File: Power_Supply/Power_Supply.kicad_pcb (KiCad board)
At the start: 2 copper layers, 100 x 100 mm, 61 parts, among them J1 ICSP, J2 Conn_01x01, J3 Conn_01x01, J4 Conn_01x02, SW1 UP, SW2 DW, SW3 V_I_SEL, SW4 O_EN, U1 L78L08_SOT89, U2 ATmega328PB-AU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

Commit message: need to add display
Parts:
- added J5: Conn_01x07, Custom_Vertical_1x_2.54mm_Pin_Header:PinHeader_1x07_P2.54mm_Vertical, F.Cu at (-13.0, 45.0)
- moved C16 145.0 mm to (66.0, 94.0), turned to 180 degrees
- moved R11 139.7 mm to (64.0, 69.0), turned to 90 degrees
- moved C18 137.9 mm to (60.0, 94.0)
- moved C6 137.4 mm to (72.4, 107.8), turned to 90 degrees
- moved R3 134.5 mm to (84.4, 101.0)
- moved C8 134.5 mm to (80.0, 101.0)
- moved R18 134.4 mm to (54.4, 96.0)
- moved C20 133.1 mm to (51.4, 92.0), turned to 90 degrees
- moved R14 130.2 mm to (73.0, 81.0), turned to 180 degrees
- moved R5 127.6 mm to (89.0, 86.9), turned to 90 degrees
- moved R20 121.6 mm to (84.0, 87.0), turned to -90 degrees
- moved R16 120.1 mm to (73.0, 85.0), turned to 180 degrees
- moved R12 119.8 mm to (73.0, 79.0)
- moved R17 119.7 mm to (73.0, 87.0)
- moved C3 117.9 mm to (80.0, 78.0)
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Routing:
- net +VSW: track 0.00 -> 53.4 mm
- net /V_FB: track 0.00 -> 17.9 mm, vias 0 -> 2
- net Net-(C16-Pad2): track 0.00 -> 17.4 mm
- net Net-(C17-Pad2): track 0.00 -> 14.4 mm
- net Net-(C15-Pad2): track 0.00 -> 14.2 mm
- net GND: track 0.00 -> 12.7 mm, vias 0 -> 4
- net Net-(C13-Pad2): track 0.00 -> 11.0 mm
- net +5V: track 0.00 -> 9.13 mm
- net Net-(C6-Pad1): track 0.00 -> 9.03 mm
- net Net-(U4-Pad3): track 0.00 -> 8.44 mm
- net Net-(R9-Pad2): track 0.00 -> 8.44 mm
- net Net-(R8-Pad2): track 0.00 -> 8.44 mm
- net Net-(R6-Pad2): track 0.00 -> 8.44 mm
- net Net-(R10-Pad2): track 0.00 -> 8.44 mm
- net Net-(R16-Pad1): track 0.00 -> 8.02 mm
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- added copper zone on F.Cu, net +VSW
- added copper zone on F.Cu, net Net-(C16-Pad2)
- added copper zone on F.Cu, net Net-(C6-Pad2)
- added copper zone on F.Cu, net Net-(R13-Pad1)
- added copper zone on F.Cu, net VDC

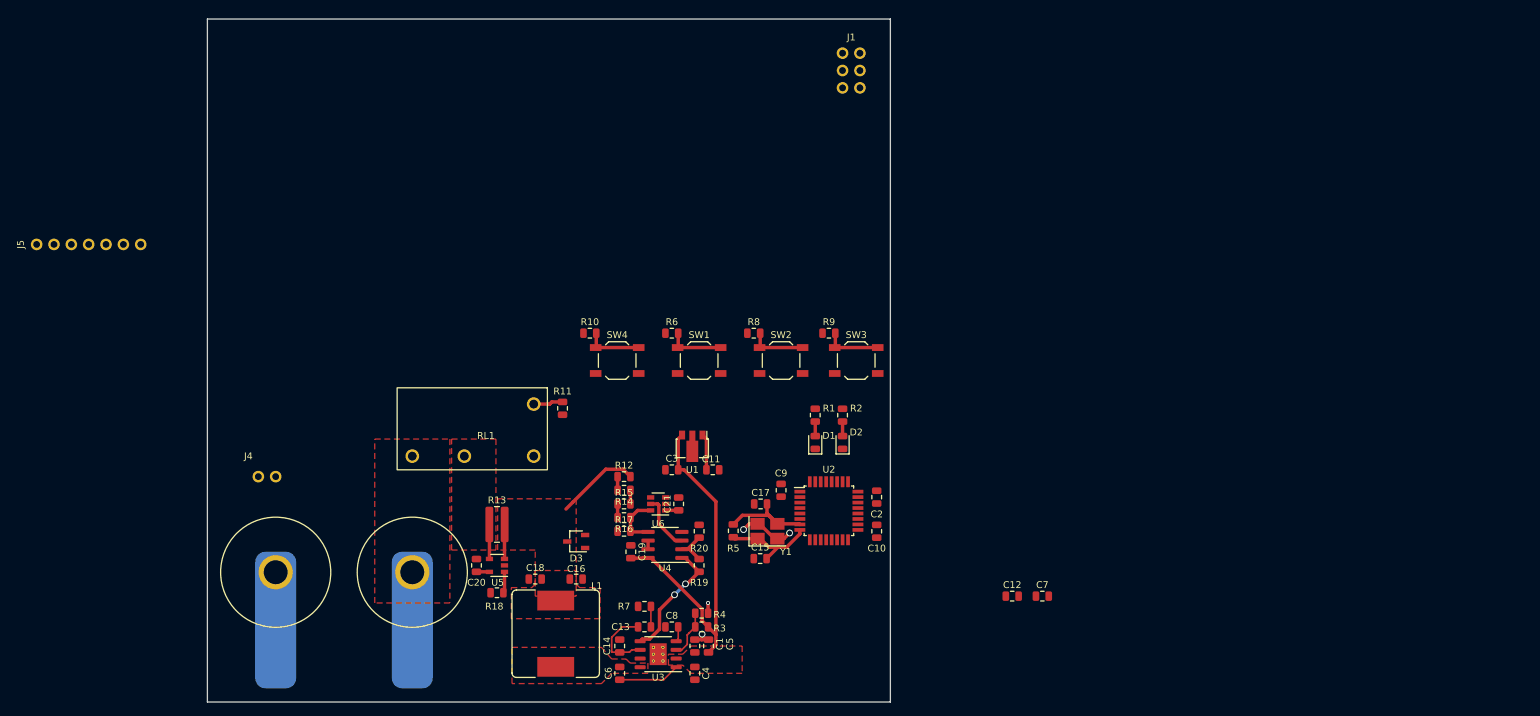
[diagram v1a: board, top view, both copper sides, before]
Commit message: layout complete - OLED missing
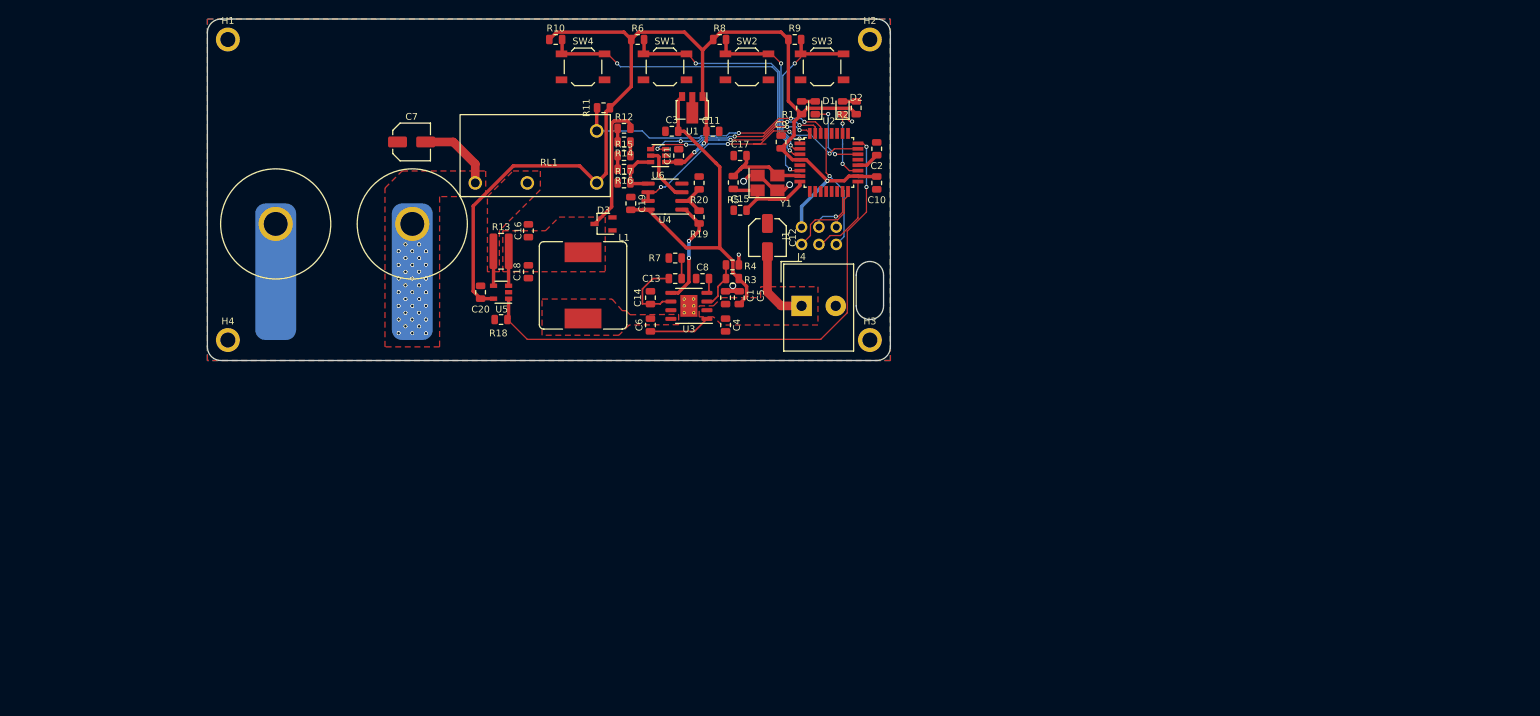
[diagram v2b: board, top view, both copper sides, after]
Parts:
- removed J5: Conn_01x07, Custom_Vertical_1x_2.54mm_Pin_Header:PinHeader_1x07_P2.54mm_Vertical
- added H1: MountingHole_Pad, MountingHole:MountingHole_2.2mm_M2_ISO7380_Pad, F.Cu at (15.0, 15.0)
- added H2: MountingHole_Pad, MountingHole:MountingHole_2.2mm_M2_ISO7380_Pad, F.Cu at (109.0, 15.0)
- added H3: MountingHole_Pad, MountingHole:MountingHole_2.2mm_M2_ISO7380_Pad, F.Cu at (109.0, 59.0)
- added H4: MountingHole_Pad, MountingHole:MountingHole_2.2mm_M2_ISO7380_Pad, F.Cu at (15.0, 59.0)
- C12, C7: value 100nF -> 10uF; footprint Capacitor_SMD:C_0805_2012Metric -> Capacitor_SMD:C_Elec_5x5.4
- J4: value Conn_01x02 -> Screw_Terminal_01x02; footprint Custom_Vertical_1x_2.54mm_Pin_Header:PinHeader_1x02_P2.54mm_Vertical -> TerminalBlock_Altech:Altech_AK300_1x02_P5.00mm_45-Degree
- moved C7 113.8 mm to (41.9, 30.0)
- moved J4 81.0 mm to (99.0, 54.0), turned to 0 degrees
- moved C12 63.6 mm to (94.0, 44.0), turned to -90 degrees
- moved C16 51.5 mm to (59.0, 43.0), turned to -90 degrees
- moved C1 51.2 mm to (87.9, 52.8)
- moved C13 51.2 mm to (80.5, 50.0)
- moved C14 51.2 mm to (76.9, 52.8)
- moved C4 51.2 mm to (87.9, 56.8)
- moved C5 51.2 mm to (89.9, 52.8)
- moved C6 51.2 mm to (76.9, 56.8)
- moved C8 51.2 mm to (84.5, 50.0)
- moved R3 51.2 mm to (88.9, 50.0)
- moved R4 51.2 mm to (88.9, 48.0)
- moved R7 51.2 mm to (80.5, 47.0)
- moved U3 51.2 mm to (82.5, 54.0)
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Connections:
- net Net-(R8-Pad2) renamed /SW2
- C12 pad 2: +5V -> +VSW
- C7 pad 2: +5V -> VDC
- J4 pad 1: VDC -> +VSW
- R10 pad 2: Net-(R10-Pad2) -> /SW4
- R6 pad 2: Net-(R6-Pad2) -> /SW1
- R9 pad 2: Net-(R9-Pad2) -> /SW3
- SW1 pad 1: Net-(R6-Pad2) -> /SW1
- SW3 pad 1: Net-(R9-Pad2) -> /SW3
- SW4 pad 1: Net-(R10-Pad2) -> /SW4
- U2 pad 1: Net-(R6-Pad2) -> /SW3
- U2 pad 10: Net-(R10-Pad2) -> Net-(U2-Pad10)
- U2 pad 3: /SDA1 -> /SW1
- U2 pad 6: /SCL1 -> /SW4
- U2 pad 9: Net-(R9-Pad2) -> Net-(U2-Pad9)
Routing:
- net +5V: track 9.13 -> 171.6 mm, vias 0 -> 3
- net /I_SENSE: track 3.12 -> 82.6 mm, vias 0 -> 2
- net /SW4: track 0.00 -> 51.4 mm, vias 0 -> 2
- net /V_SENSE: track 1.27 -> 40.3 mm, vias 0 -> 4
- net /SW1: track 0.00 -> 37.1 mm, vias 0 -> 2
- net /~RLY_CNTRL: track 4.35 -> 39.3 mm, vias 0 -> 3
- net /POT_U~D: track 0.00 -> 27.2 mm, vias 0 -> 5
- net /~POT_CS: track 0.00 -> 26.0 mm, vias 0 -> 4
- net /SW3: track 0.00 -> 24.4 mm, vias 0 -> 2
- net /RST: track 0.00 -> 17.8 mm, vias 0 -> 1
- net /SW2: track 8.44 -> 25.0 mm, vias 0 -> 2
- net /SCK: track 0.00 -> 12.7 mm
- net /MISO: track 0.00 -> 12.5 mm
- net Net-(D2-Pad1): track 0.00 -> 11.9 mm, vias 0 -> 3
- net Net-(D1-Pad1): track 0.00 -> 11.7 mm, vias 0 -> 2
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- added copper zone on B.Cu, net GND
- added copper zone on F.Cu, net GND
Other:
- board size 100 x 100 mm -> 100 x 50 mm
